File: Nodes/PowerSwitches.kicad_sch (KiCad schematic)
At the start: 48 parts, among them IC1 VNQ9080AJTR, IC2 VNQ9080AJTR, T21 Conn_01x01, T22 Conn_01x01

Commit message: Nodes v2.2.5
- New High-Side Driver (Same footprint, just new info)
- Two resistors added for 3V3 Filters, which can be used to implement voltage divider
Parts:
- IC1, IC2: value VNQ9080AJTR -> VNQ9025AJTR; DATASHEET LINK https://www.st.com/resource/en/datasheet/vnq9080aj.pdf -> https://www.st.com/resource/en/datasheet/vnq9025aj.pdf; MANUFACTURER_PART_NUMBER VNQ9080AJTR -> VNQ9025AJTR; MOUSER PART NUMBER 511-VNQ9080AJTR -> 511-VNQ9025AJTR; MOUSER PRICE/STOCK https://www.mouser.co.uk/ProductDetail/STMicroelectronics/V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 -> (none)
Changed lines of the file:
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@@
 			)
 		)
-		(property "Value" "VNQ9080AJTR"
+		(property "Value" "VNQ9025AJTR"
 			(at 110.49 72.898 0)
 			(effects
@@
 			)
 		)
-		(property "DATASHEET LINK" "https://www.st.com/resource/en/datasheet/vnq9080aj.pdf"
+		(property "DATASHEET LINK" "https://www.st.com/resource/en/datasheet/vnq9025aj.pdf"
 			(at 104.902 34.29 0)
 			(effects
@@
 			)
 		)
-		(property "MANUFACTURER_PART_NUMBER" "VNQ9080AJTR"
+		(property "MANUFACTURER_PART_NUMBER" "VNQ9025AJTR"
 			(at 104.902 34.29 0)
 			(effects
@@
 			)
 		)
-		(property "MOUSER PART NUMBER" "511-VNQ9080AJTR"
+		(property "MOUSER PART NUMBER" "511-VNQ9025AJTR"
 			(at 104.902 34.29 0)
 			(effects
@@
 			)
 		)
-		(property "MOUSER PRICE/STOCK" "https://www.mouser.co.uk/ProductDetail/STMicroelectronics/VNQ9080AJTR?qs=MyNHzdoqoQKvlnwVdNzF7A%3D%3D"
+		(property "MOUSER PRICE/STOCK" ""
 			(at 104.902 34.29 0)
 			(effects
@@
 			)
 		)
-		(property "Value" "VNQ9080AJTR"
+		(property "Value" "VNQ9025AJTR"
 			(at 110.49 144.018 0)
 			(effects
@@
 			)
 		)
-		(property "DATASHEET LINK" "https://www.st.com/resource/en/datasheet/vnq9080aj.pdf"
+		(property "DATASHEET LINK" "https://www.st.com/resource/en/datasheet/vnq9025aj.pdf"
 			(at 104.902 105.41 0)
 			(effects
@@
 			)
 		)
-		(property "MANUFACTURER_PART_NUMBER" "VNQ9080AJTR"
+		(property "MANUFACTURER_PART_NUMBER" "VNQ9025AJTR"
 			(at 104.902 105.41 0)
 			(effects
@@
 			)
 		)
-		(property "MOUSER PART NUMBER" "511-VNQ9080AJTR"
+		(property "MOUSER PART NUMBER" "511-VNQ9025AJTR"
 			(at 104.902 105.41 0)
 			(effects
@@
 			)
 		)
-		(property "MOUSER PRICE/STOCK" "https://www.mouser.co.uk/ProductDetail/STMicroelectronics/VNQ9080AJTR?qs=MyNHzdoqoQKvlnwVdNzF7A%3D%3D"
+		(property "MOUSER PRICE/STOCK" ""
 			(at 104.902 105.41 0)
 			(effects

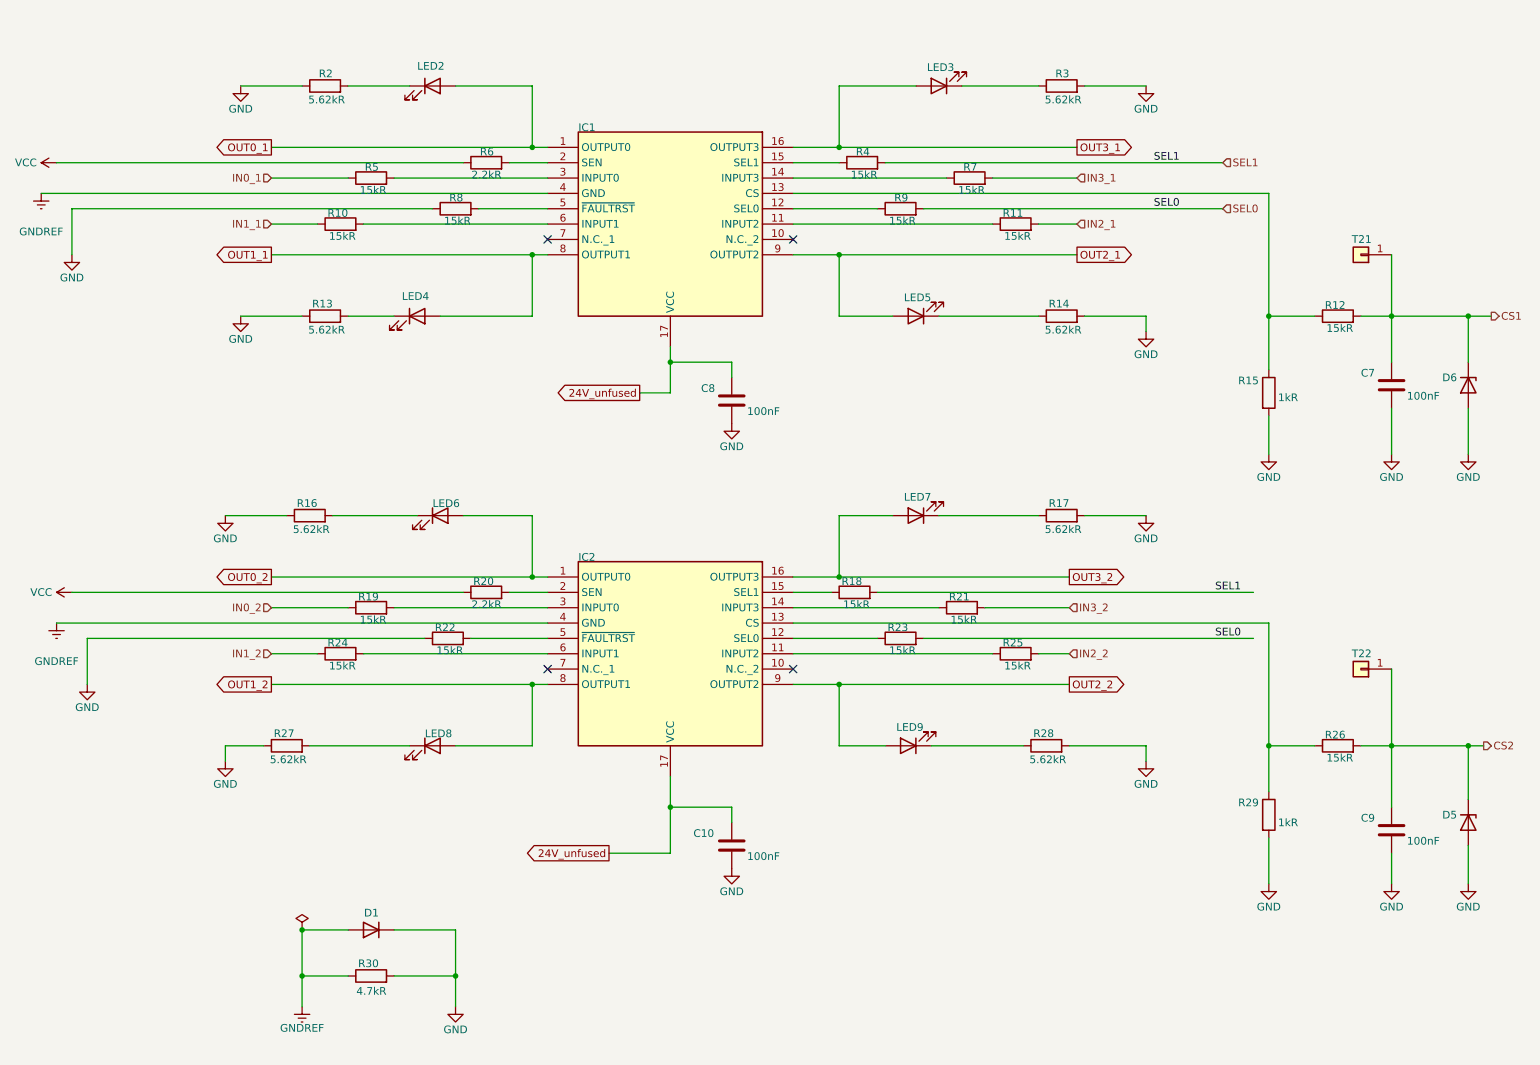
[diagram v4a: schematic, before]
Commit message: Nodes 2.2.5 Revision 1
- New LED colour coding
- Nodes Datasheet added
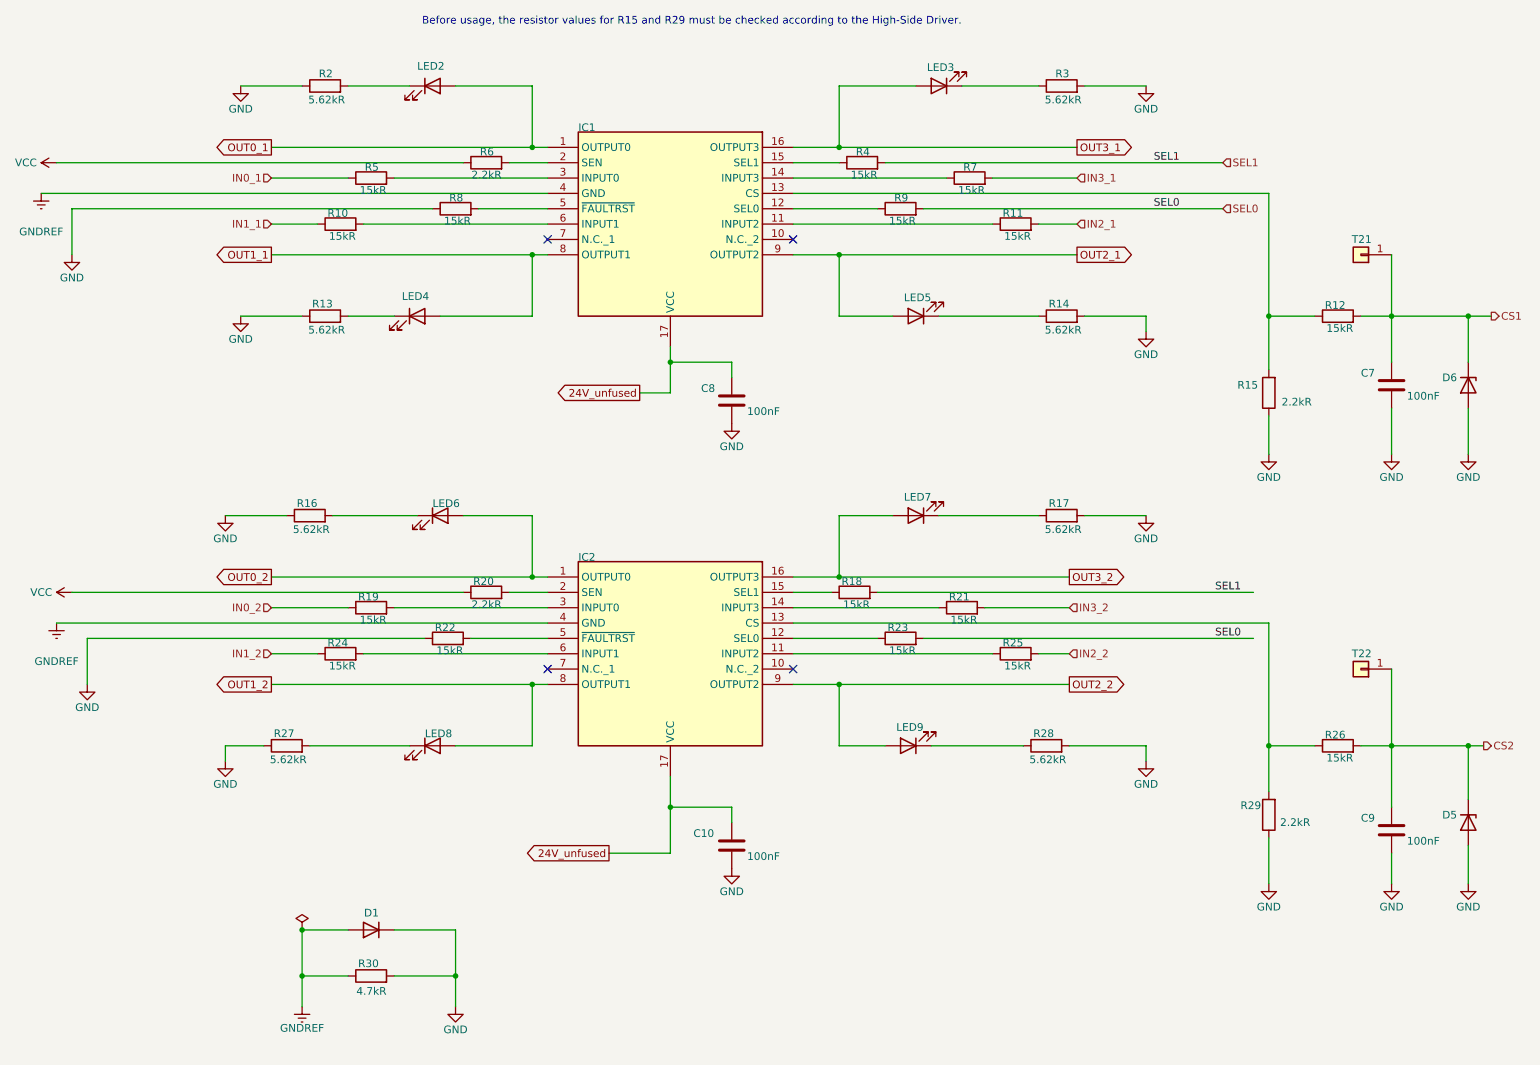
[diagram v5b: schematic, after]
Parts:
- R15, R29: value 1kR -> 2.2kR; ALTIUM_VALUE (none) -> 2.2kR; CASE/PACKAGE (none) -> 0805; CONSTRUCTION (none) -> Chip; JESD-609 CODE (none) -> e3; MAX OPERATING TEMPERATURE (none) -> 155°C; MIN OPERATING TEMPERATURE (none) -> -55°C; MOUNTING TECHNOLOGY (none) -> Surface Mount; PACKAGE HEIGHT (none) -> 0.5mm; PACKAGE LENGTH (none) -> 2mm; PACKAGE SHAPE (none) -> Rectangular; PACKAGE STYLE (none) -> SMTMeter; PACKAGE WIDTH (none) -> 1.25mm; PACKAGING (none) -> Tape and Reel; PINS (none) -> 2; POWER (none) -> 125mW; RATED TEMPERATURE (none) -> 70°C; REACH SVHC COMPLIANT (none) -> Yes; RESISTOR TYPE (none) -> FIXED RESISTOR; ROHS COMPLIANT (none) -> Yes; TECHNOLOGY (none) -> RUTHENIUM OXIDE; TEMPERATURE COEFFICIENT (none) -> 100ppm/°C; TERMINAL FINISH (none) -> Nickel; TERMINATION (none) -> Wraparound; TOLERANCE (none) -> 1%; WORKING VOLTAGE (none) -> 150V
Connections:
- net GND: now also R15.1, R29.1; no longer R15.2, R29.2
- net at IC1.13 (CS), R12.1: now also R15.2; no longer R15.1
- net at IC2.13 (CS), R26.1: now also R29.2; no longer R29.1
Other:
- note added: "Before usage, the resistor values for R15 and R29 ​​must be checked according to the High-Side Driver."
